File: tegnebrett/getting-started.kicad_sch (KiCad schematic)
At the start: 31 parts, among them J1 FH12-45S-0.5SH55, J2 FH12-6S-1SH55, J3 Conn_ST_STDC14, SW1 SW_Push, SW2 SW_Push, SW3 SW_Push, U5 STM32U5G7VJTxQ, Y1 60MHz

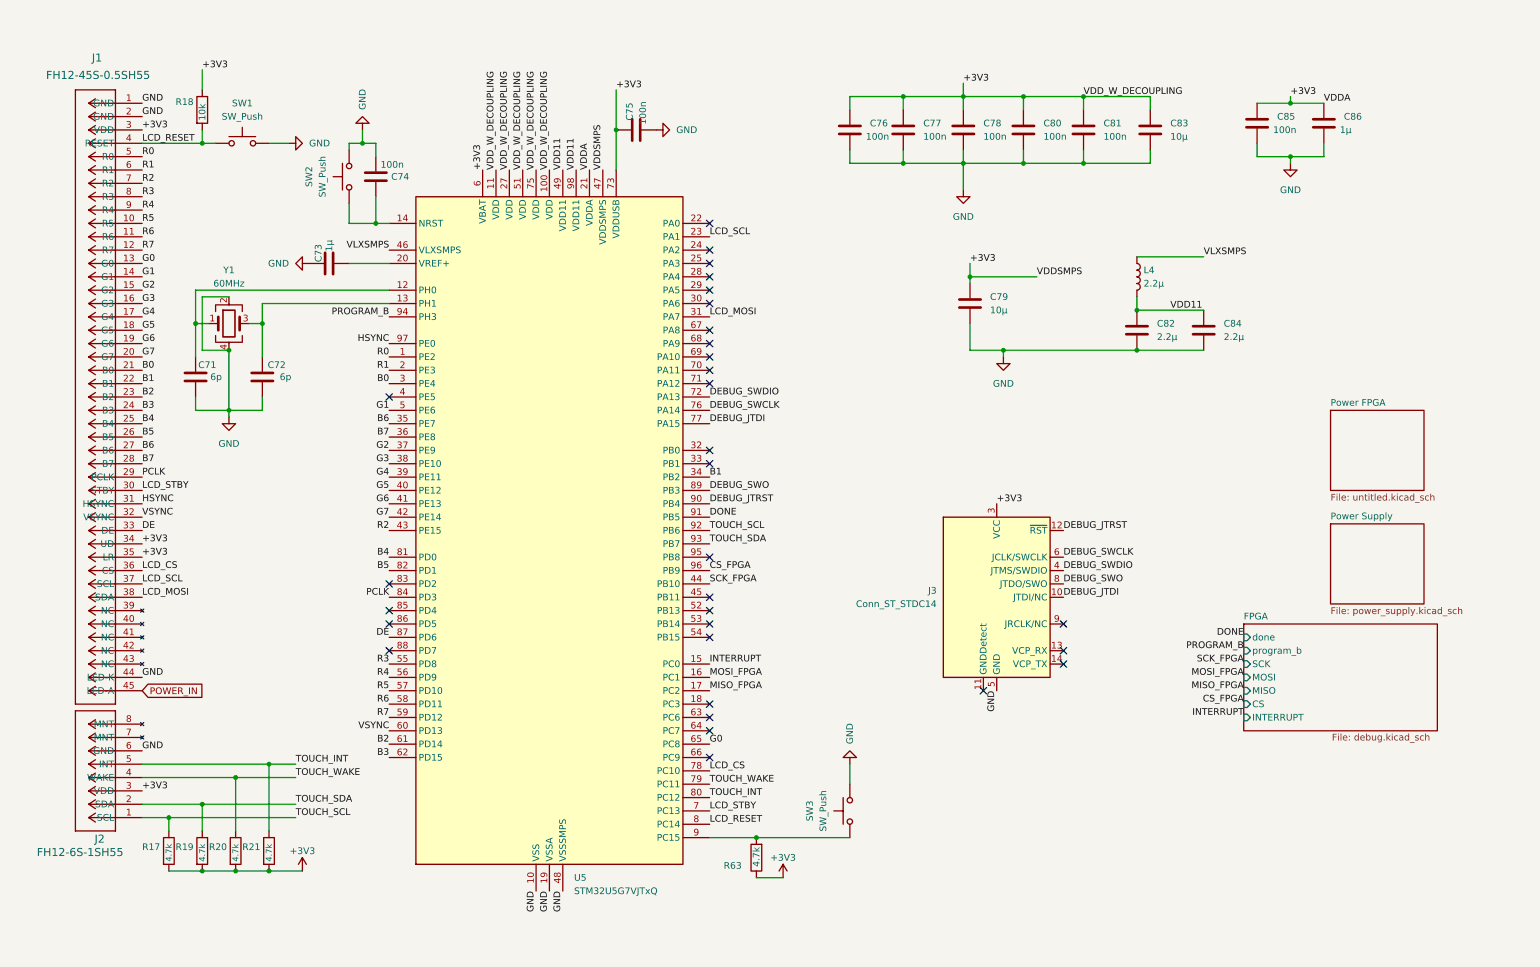
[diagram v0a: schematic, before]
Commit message: feat: PCB update
Main additions:

- Added LEDs to Power Supply, MCU and FPGA.
The resistor values will depend on the specific LEDs we buy.
Red LEDs need a different resistor value than blue LEDs, etc.

- Added a bunch of buttons to the MCU
It doesn't hurt to have some redundancy here.

- Added header pins
Allows us to easily reach GPIO pins on the MCU and the FPGA.
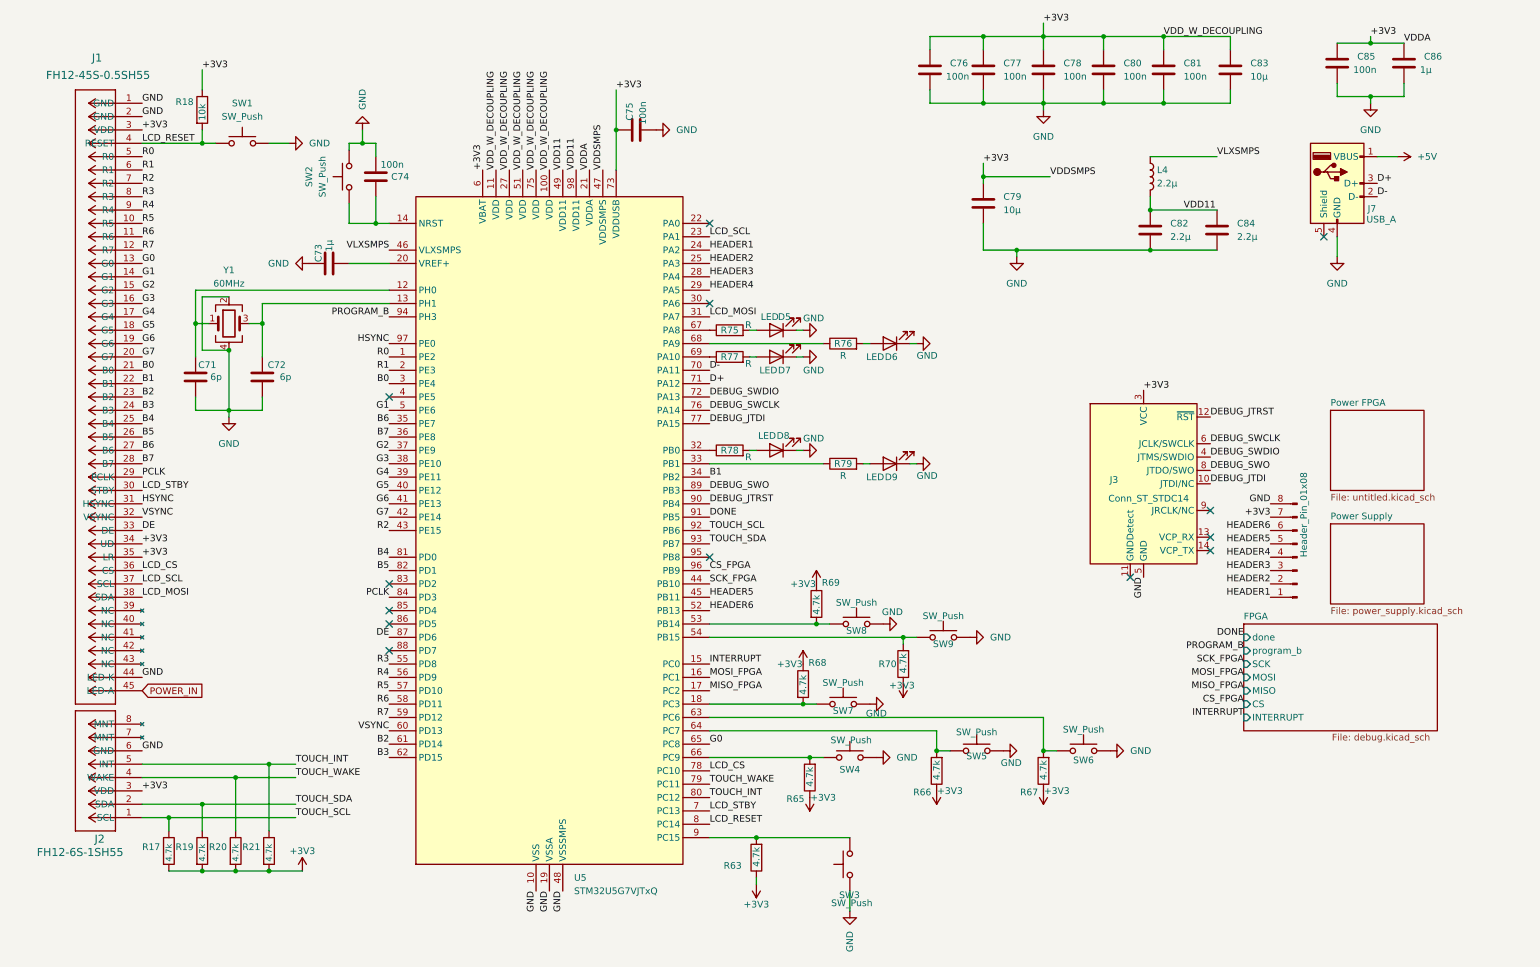
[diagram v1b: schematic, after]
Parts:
- added D5, D6, D7, D8, D9: LED, symbol Device:LED
- added J5: Header_Pin_01x08, symbol Connector:Conn_01x08_Pin
- added J7: USB_A, symbol Connector:USB_A
- added R65, R66, R67, R68, R69, R70: 4.7k, symbol Device:R
- added R75, R76, R77, R78, R79: R, symbol Device:R
- added SW4, SW5, SW6, SW7, SW8, SW9: SW_Push, symbol Switch:SW_Push
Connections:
- net +3V3: now also J5.7 (Pin_7), R65.1, R66.1, R67.1, R68.1, R69.1, R70.1
- net GND: now also SW3.1, D5.1 (K), D6.1 (K), D7.1 (K), D8.1 (K), D9.1 (K), J5.8 (Pin_8), J7.4 (GND), SW4.2, SW5.2, SW6.2, SW7.2, SW8.2, SW9.2; no longer SW3.2
- net at R63.2, U5.9 (PC15): now also SW3.2; no longer SW3.1
- net at U5.18 (PC3): now also R68.2, SW7.1
- net HEADER1: now reaches U5.24 (PA2)
- net HEADER1: now also J5.1 (Pin_1)
- net HEADER2: now reaches U5.25 (PA3)
- net HEADER2: now also J5.2 (Pin_2)
- net HEADER3: now reaches U5.28 (PA4)
- net HEADER3: now also J5.3 (Pin_3)
- net HEADER4: now reaches U5.29 (PA5)
- net HEADER4: now also J5.4 (Pin_4)
- net at U5.32 (PB0): now also R78.1
- net at U5.33 (PB1): now also R79.1
- net HEADER5: now reaches U5.45 (PB11)
- net HEADER5: now also J5.5 (Pin_5)
- net HEADER6: now reaches U5.52 (PB13)
- net HEADER6: now also J5.6 (Pin_6)
- net at U5.53 (PB14): now also R69.2, SW8.1
- net at U5.54 (PB15): now also R70.2, SW9.1
- net at U5.63 (PC6): now also R67.2, SW6.1
- net at U5.64 (PC7): now also R66.2, SW5.1
- net at U5.66 (PC9): now also R65.2, SW4.1
- net at U5.67 (PA8): now also R75.1
- net at U5.68 (PA9): now also R76.1
- net at U5.69 (PA10): now also R77.1
- net D-: now reaches U5.70 (PA11)
- net D-: now also J7.2 (D-)
- net D+: now reaches U5.71 (PA12)
- net D+: now also J7.3 (D+)
- new net: D6.2 (A), R76.2
- new net: D5.2 (A), R75.2
- new net: D8.2 (A), R78.2
- new net: D7.2 (A), R77.2
- new net: D9.2 (A), R79.2
- new net +5V: J7.1 (VBUS)
- no-connect marks 31 -> 13
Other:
- moved on the sheet: C76, C77, C78, C79, C80, C81, C82, C83, C84, C85, C86, J3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

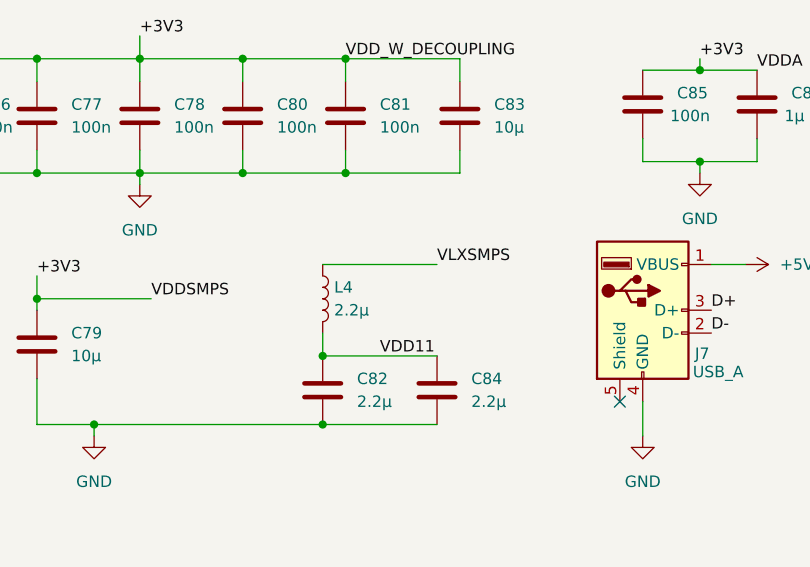
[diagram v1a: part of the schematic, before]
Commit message: feat(PCB-schematic): add power flags
This removes a lot of the warnings we're getting from the ERC checker.
There are still some warnings on the PSU, probably because we've set the
wrong pin type on some of the pins.
For example output instead of power output, etc.
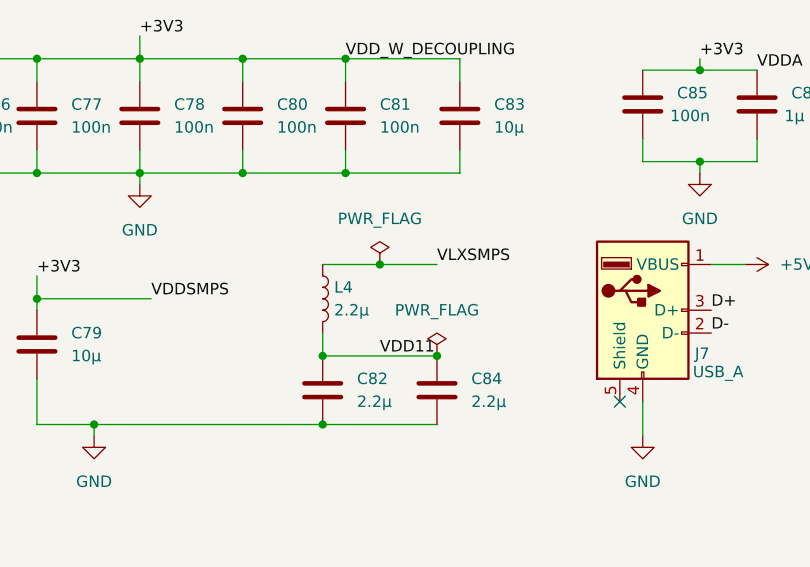
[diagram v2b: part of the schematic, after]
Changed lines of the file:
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@@
 	)
 	(junction
+		(at 241.3 50.8)
+		(diameter 0)
+		(color 0 0 0 0)
+	)
+	(junction
 		(at 54.61 176.53)
 		(diameter 0)
@@
 	)
 	(junction
+		(at 234.95 40.64)
+		(diameter 0)
+		(color 0 0 0 0)
+	)
+	(junction
 		(at 78.74 38.1)
 		(diameter 0)
@@
 	(wire
 		(pts
-			(xy 271.78 40.64) (xy 275.59 40.64)
-		)
-		(stroke
-			(width 0)
-			(type default)
-		)
-	)
-	(wire
-		(pts
 			(xy 264.16 26.67) (xy 264.16 29.21)
 		)
@@
 	(wire
 		(pts
-			(xy 228.6 40.64) (xy 241.3 40.64)
+			(xy 228.6 40.64) (xy 234.95 40.64)
 		)
 		(stroke
@@
 	(wire
 		(pts
+			(xy 234.95 40.64) (xy 241.3 40.64)
+		)
+		(stroke
+			(width 0)
+			(type default)
+		)
+	)
+	(wire
+		(pts
 			(xy 76.2 39.37) (xy 76.2 38.1)
 		)
@@
 	(wire
 		(pts
+			(xy 271.78 40.64) (xy 275.59 40.64)
+		)
+		(stroke
+			(width 0)
+			(type default)
+		)
+	)
+	(wire
+		(pts
 			(xy 67.31 176.53) (xy 60.96 176.53)
 		)
@@
 	)
 	(symbol
+		(lib_id "power:PWR_FLAG")
+		(at 241.3 50.8 0)
+		(unit 1)
+		(exclude_from_sim no)
+		(in_bom yes)
+		(on_board yes)
+		(dnp no)
+		(fields_autoplaced yes)
+		(property "Reference" "#FLG04"
+			(at 241.3 48.895 0)
+			(effects
+				(font
+					(size 1.27 1.27)
+				)
+				(hide yes)
+			)
+		)
+		(property "Value" "PWR_FLAG"
+			(at 241.3 45.72 0)
+			(effects
+				(font
+					(size 1.27 1.27)
+				)
+			)
+		)
+		(property "Footprint" ""
+			(at 241.3 50.8 0)
+			(effects
+				(font
+					(size 1.27 1.27)
+				)
+				(hide yes)
+			)
+		)
+		(property "Datasheet" "~"
+			(at 241.3 50.8 0)
+			(effects
+				(font
+					(size 1.27 1.27)
+				)
+				(hide yes)
+			)
+		)
+		(property "Description" "Special symbol for telling ERC where power comes from"
+			(at 241.3 50.8 0)
+			(effects
+				(font
+					(size 1.27 1.27)
+				)
+				(hide yes)
+			)
+		)
+		(pin "1"
+		)
+		(instances
+			(project "getting-started"
+				(path "/d9a31669-c5f1-42a7-9461-3df04b9a4e62"
+					(reference "#FLG04")
+					(unit 1)
+				)
+			)
+		)
+	)
+	(symbol
 		(lib_id "Device:R")
 		(at 187.96 157.48 180)
@@
 					(unit 1)
 				)
+			)
+		)
+	)
+	(symbol
+		(lib_id "power:PWR_FLAG")
+		(at 234.95 40.64 0)
+		(unit 1)
+		(exclude_from_sim no)
+		(in_bom yes)
+		(on_board yes)
+		(dnp no)
+		(fields_autoplaced yes)
+		(property "Reference" "#FLG05"
+			(at 234.95 38.735 0)
+			(effects
+				(font
+					(size 1.27 1.27)
+				)
+				(hide yes)
+			)
+		)
+		(property "Value" "PWR_FLAG"
+			(at 234.95 35.56 0)
+			(effects
+				(font
+					(size 1.27 1.27)
+				)
+			)
+		)
+		(property "Footprint" ""
+			(at 234.95 40.64 0)
+			(effects
+				(font
+					(size 1.27 1.27)
+				)
+				(hide yes)
+			)
+		)
+		(property "Datasheet" "~"
+			(at 234.95 40.64 0)
+			(effects
+				(font
+					(size 1.27 1.27)
+				)
+				(hide yes)
+			)
+		)
+		(property "Description" "Special symbol for telling ERC where power comes from"
+			(at 234.95 40.64 0)
+			(effects
+				(font
+					(size 1.27 1.27)
+				)
+				(hide yes)
+			)
+		)
+		(pin "1"
+		)
+		(instances
+			(project "getting-started"
+				(path "/d9a31669-c5f1-42a7-9461-3df04b9a4e62"
+					(reference "#FLG05")
+					(unit 1)
+				)

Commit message: feat: added PCB file
Placed the 45-pin connector and connected the 3D_model for it to the
footprint.
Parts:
- J1: footprint hirose-footprints:CONN_45S-0.5SH55 -> tegnebrett_modules:CONN_45S-0.5SH55
- J2: footprint hirose-footprints:CON6_1X6_DRBF_HST_HIR -> tegnebrett_modules:CON6_1X6_DRBF_HST_HIR
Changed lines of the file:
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@@
 			)
 		)
-		(property "Footprint" "hirose-footprints:CON6_1X6_DRBF_HST_HIR"
+		(property "Footprint" "tegnebrett_modules:CON6_1X6_DRBF_HST_HIR"
 			(at 36.83 166.37 0)
 			(effects
@@
 		)
 		(property "Sim.Library" "./"
+			(at 36.83 166.37 0)
+			(effects
+				(font
+					(size 1.27 1.27)
+				)
+				(hide yes)
+			)
+		)
+		(property "Sim.Name" "<unbekannt>"
 			(at 36.83 166.37 0)
 			(effects
@@
 			)
 		)
-		(property "Footprint" "hirose-footprints:CONN_45S-0.5SH55"
+		(property "Footprint" "tegnebrett_modules:CONN_45S-0.5SH55"
 			(at 33.782 21.336 0)
 			(effects
@@
 			(at 36.83 30.48 0)
 			(effects
+				(font
+					(size 1.27 1.27)
+				)
+				(hide yes)
+			)
+		)
+		(property "Sim.Library" "./"
+			(at 36.83 30.48 0)
+			(effects

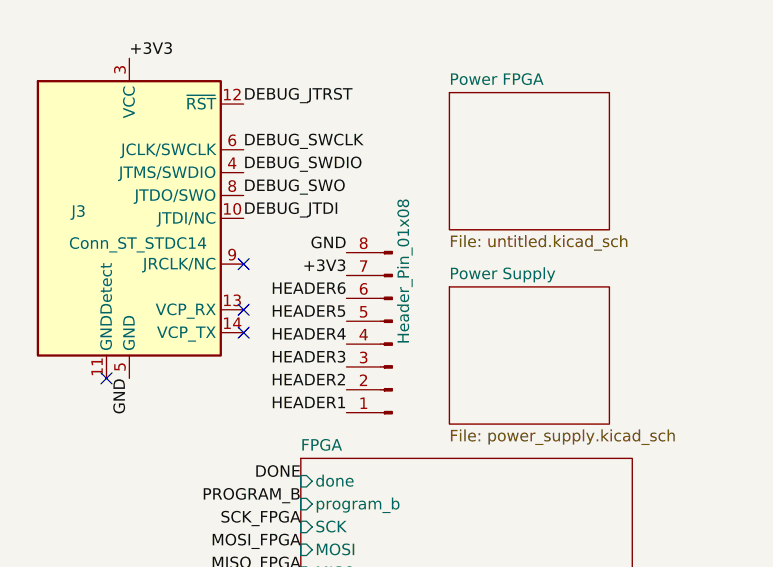
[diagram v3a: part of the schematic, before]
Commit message: feat: add some footprints
Added footprints to vertical 8pin connectors and so forth.
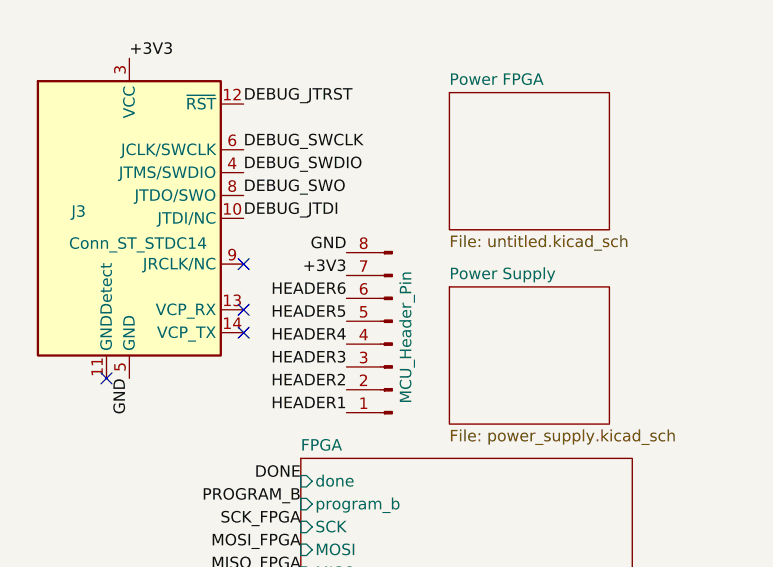
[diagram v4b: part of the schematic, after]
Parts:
- J3: footprint (none) -> Connector_PinHeader_1.27mm:PinHeader_2x07_P1.27mm_Vertical
- J5: value Header_Pin_01x08 -> MCU_Header_Pin; footprint (none) -> Connector_PinHeader_2.54mm:PinHeader_1x08_P2.54mm_Vertical
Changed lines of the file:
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@@
 			)
 		)
-		(property "Footprint" ""
+		(property "Footprint" "Connector_PinHeader_1.27mm:PinHeader_2x07_P1.27mm_Vertical"
 			(at 227.33 102.87 0)
 			(effects
@@
 			)
 		)
-		(property "Value" "Header_Pin_01x08"
-			(at 257.81 116.8399 90)
+		(property "Value" "MCU_Header_Pin"
+			(at 258.064 123.444 90)
 			(effects
 				(font
@@
 			)
 		)
-		(property "Footprint" ""
+		(property "Footprint" "Connector_PinHeader_2.54mm:PinHeader_1x08_P2.54mm_Vertical"
 			(at 256.54 116.84 0)
 			(effects
